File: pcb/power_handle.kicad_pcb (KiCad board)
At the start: 2 copper layers, 115 x 32 mm, 58 parts, among them J1 PJ-202A, J2 USB_C_Receptacle_USB2.0, Q1 PSMN6R0-25YLB, Q2 PSMN6R0-25YLB, Q3 BSS214NW, SW1 SW_SPST, U1 MCP73831T-2ATI/OT, U2 PAM2423, U3 BQ29703DSET

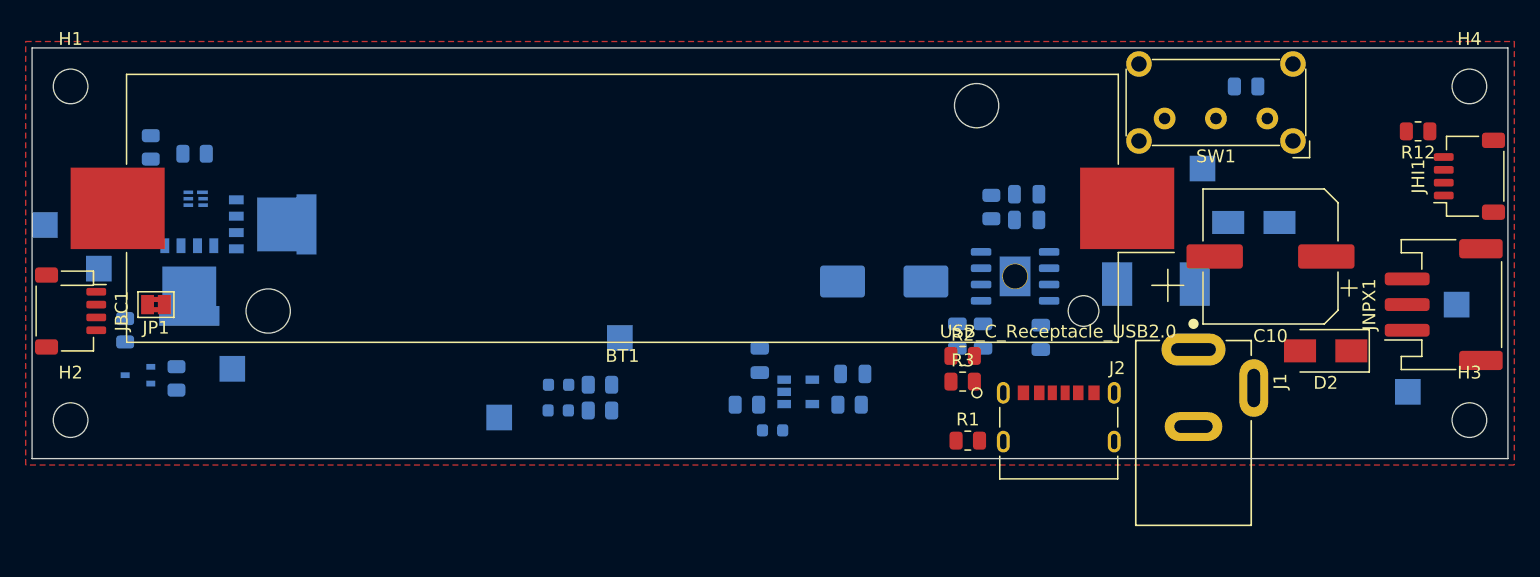
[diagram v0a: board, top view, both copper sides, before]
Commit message: pcb: redo power handle layout
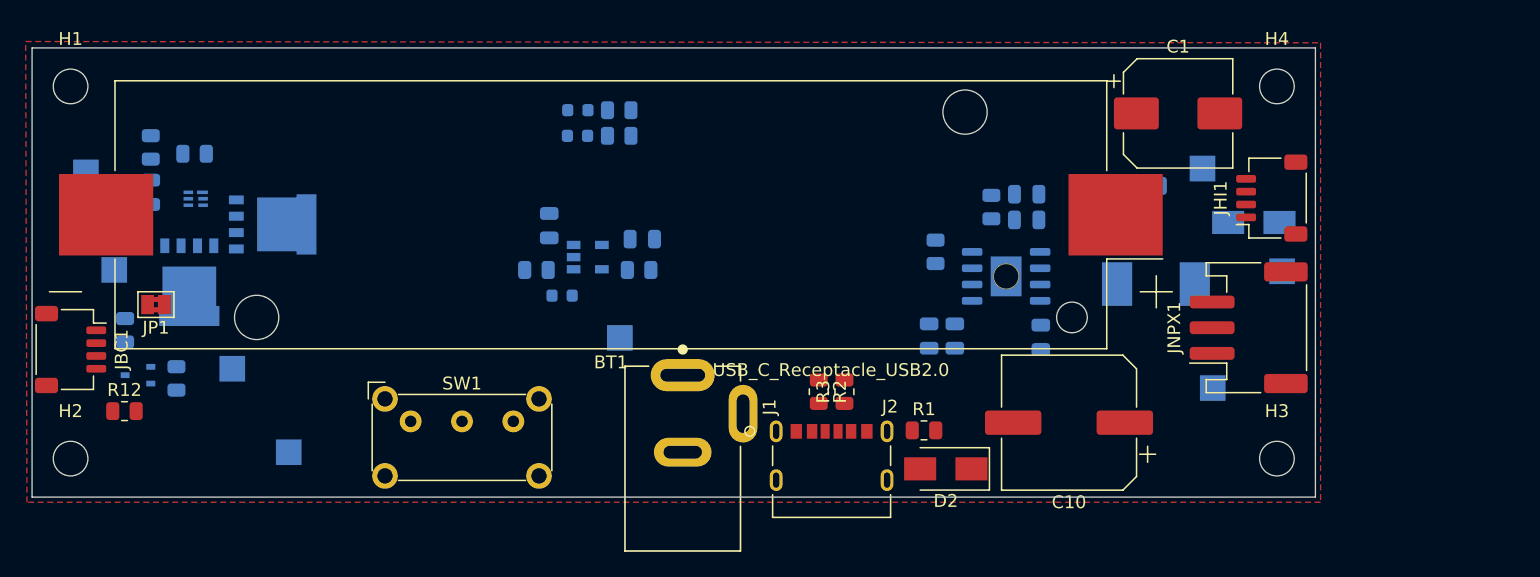
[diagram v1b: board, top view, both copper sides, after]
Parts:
- C1: moved to F.Cu
- moved R12 103.1 mm to (7.20, 28.3), turned to 0 degrees
- moved SW1 70.8 mm to (29.5, 29.1), turned to 0 degrees
- moved J1 39.9 mm to (50.7, 32.0)
- moved D2 31.0 mm to (71.2, 32.8)
- moved R5 27.4 mm to (70.4, 15.9), turned to 270 degrees
- moved C1 26.4 mm to (89.3, 5.10), turned to 0 degrees
- moved D5 21.5 mm to (42.5, 6.85)
- moved D6 21.5 mm to (42.5, 4.85)
- moved R15 21.5 mm to (45.8, 6.85)
- moved R16 21.5 mm to (45.8, 4.85)
- moved C10 20.4 mm to (80.8, 29.2)
- moved C6 19.5 mm to (47.5, 14.9)
- moved C7 19.5 mm to (40.3, 13.8)
- moved D3 19.5 mm to (41.3, 19.3)
- moved R4 19.5 mm to (47.3, 17.3)
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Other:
- board size 115 x 32 mm -> 100 x 35 mm

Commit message: pcb: finish routing of power handle
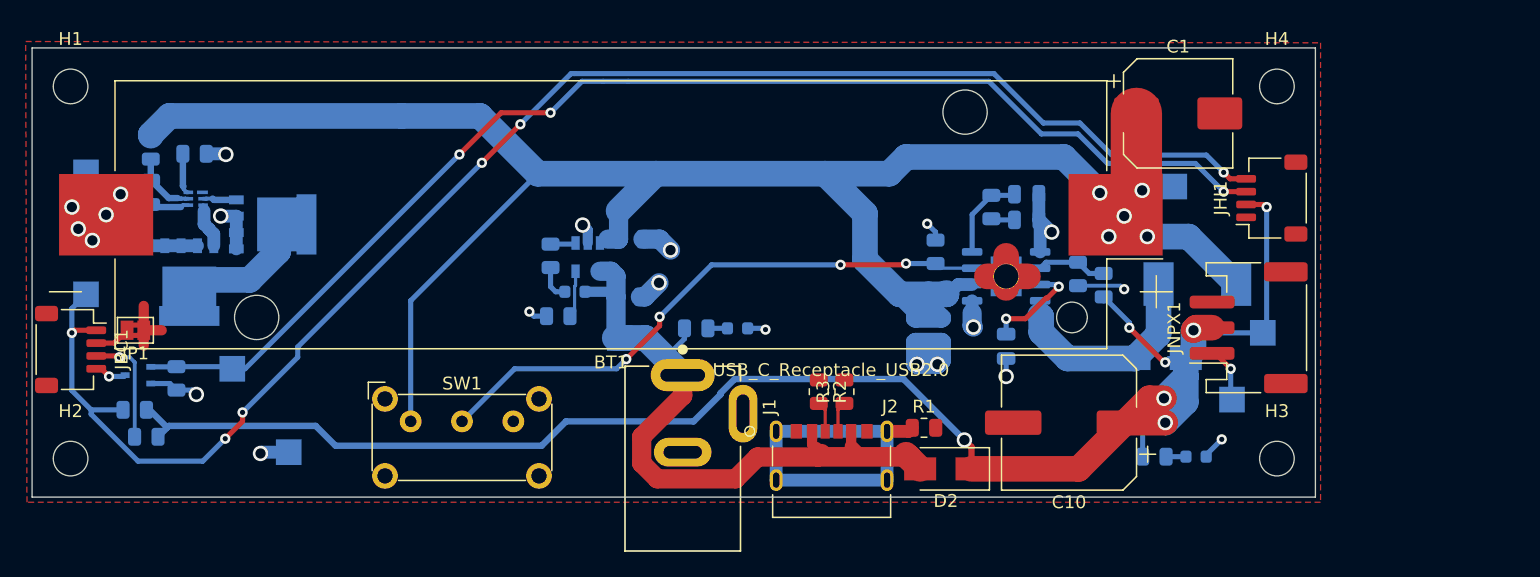
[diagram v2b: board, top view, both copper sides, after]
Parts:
- R12: moved to B.Cu
- moved D5 54.3 mm to (90.7, 31.9), turned to 180 degrees
- moved R15 48.6 mm to (87.5, 31.9), turned to 180 degrees
- moved D6 21.1 mm to (55.0, 21.9), turned to 180 degrees
- moved R16 18.0 mm to (51.8, 21.9), turned to 180 degrees
- moved D4 12.9 mm to (87.9, 24.2)
- moved R9 8.79 mm to (81.5, 17.6), turned to 90 degrees
- moved R13 8.46 mm to (8.90, 30.3), turned to 0 degrees
- moved R8 7.74 mm to (83.5, 18.5), turned to 270 degrees
- moved R4 7.26 mm to (41.0, 20.9), turned to 180 degrees
- moved C7 6.44 mm to (46.6, 14.9), turned to 0 degrees
- moved TP1 5.03 mm to (95.9, 22.2)
- moved C6 4.63 mm to (46.5, 19.4)
- moved L1 3.22 mm to (90.8, 18.4)
- moved TP6 2.91 mm to (4.20, 19.2)
- moved C8 2.79 mm to (75.9, 23.2)
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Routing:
- net +BATT: track 0.00 -> 164.3 mm, vias 0 -> 5
- net VCC: track 0.00 -> 135.5 mm, vias 0 -> 7
- net BTN+: track 0.00 -> 123.2 mm, vias 0 -> 6
- net IC_BTN_LED: track 0.00 -> 98.3 mm, vias 0 -> 3
- net VBUS: track 0.00 -> 62.7 mm
- net GND: track 0.00 -> 56.9 mm, vias 0 -> 17
- net OUTEN: track 0.00 -> 45.5 mm, vias 0 -> 4
- net -BATT: track 0.00 -> 27.9 mm, vias 0 -> 5
- net Net-(J2-PadS1): track 0.00 -> 27.0 mm
- net Net-(D4-Pad2): track 0.00 -> 17.4 mm
- net Net-(Q1-Pad5): track 0.00 -> 10.2 mm
- net LED+: track 0.00 -> 9.01 mm, vias 0 -> 1
- net Net-(C8-Pad2): track 0.00 -> 7.85 mm, vias 0 -> 2
- net Net-(C5-Pad1): track 0.00 -> 6.87 mm
- net Net-(R8-Pad1): track 0.00 -> 5.51 mm
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
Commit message: pcb: cleanup power handle silkscreen, edge cuts
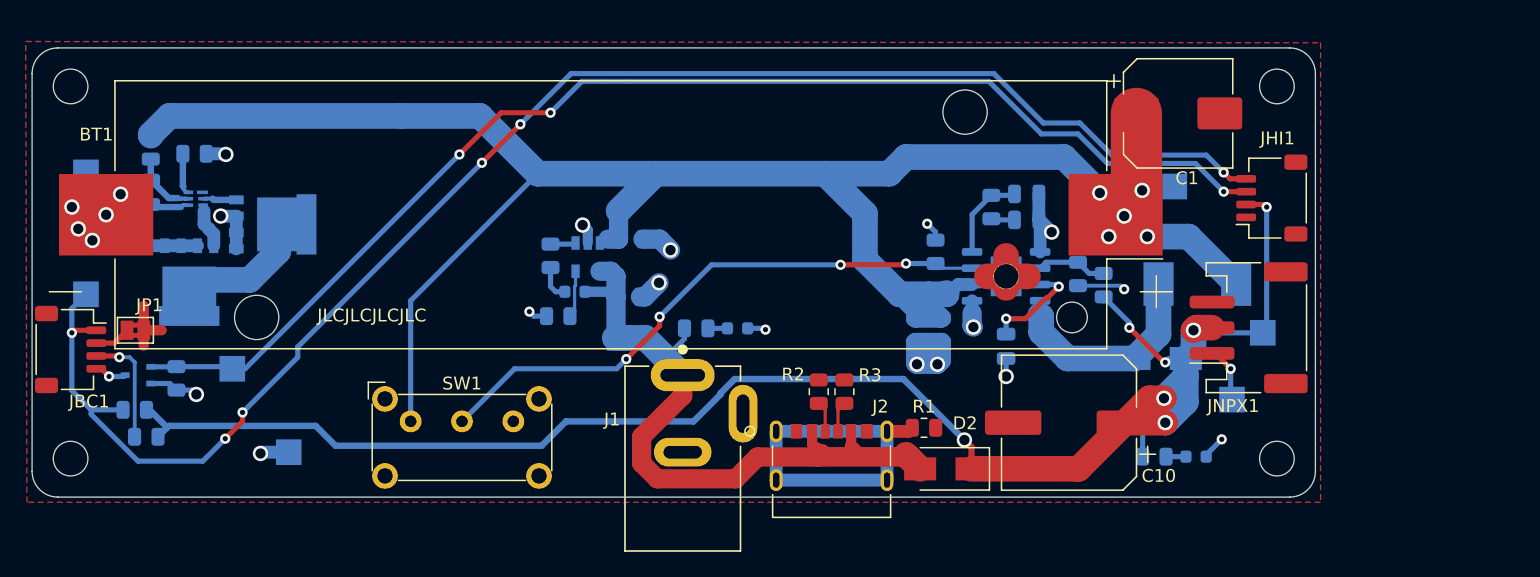
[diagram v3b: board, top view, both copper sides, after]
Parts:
- added LOGO1: Logo_Open_Hardware_Small, Symbol:OSHW-Logo_5.7x6mm_SilkScreen, B.Cu at (27.1, 6.28)
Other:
- outline, holes or cut-outs redrawn
- board text added: "JLCJLCJLCJLC"
- board text added: "LitePog Power Board Rev 1 For use with unprotected cells"

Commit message: pcb: Add testpoint labels to power handle
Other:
- board text added: "+BATT"
- board text added: "-BATT"
- board text added: "BTN+"
- board text added: "GND"
- board text added: "IC_BTN_LED"
- board text added: "NPX_DATA"
- board text added: "VBUS"
- board text added: "VCC 5V"

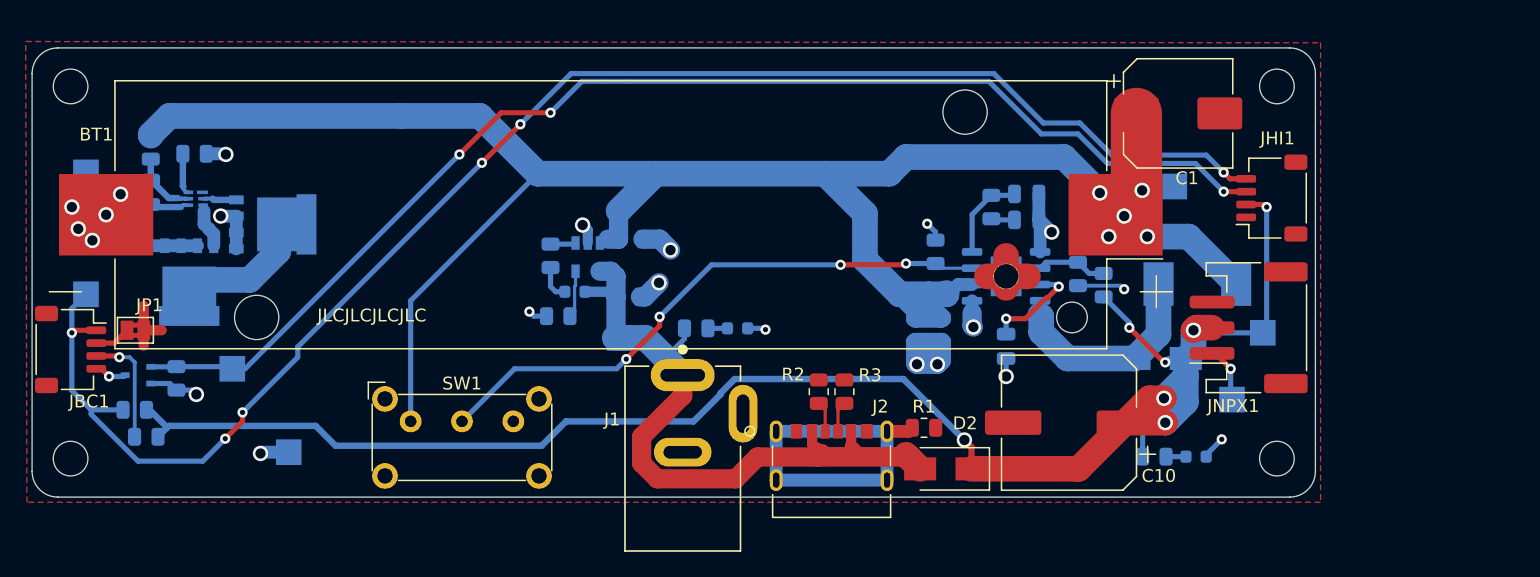
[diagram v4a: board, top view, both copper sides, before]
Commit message: power_handle: Add second ground layer, more info on silkscreen (#3)
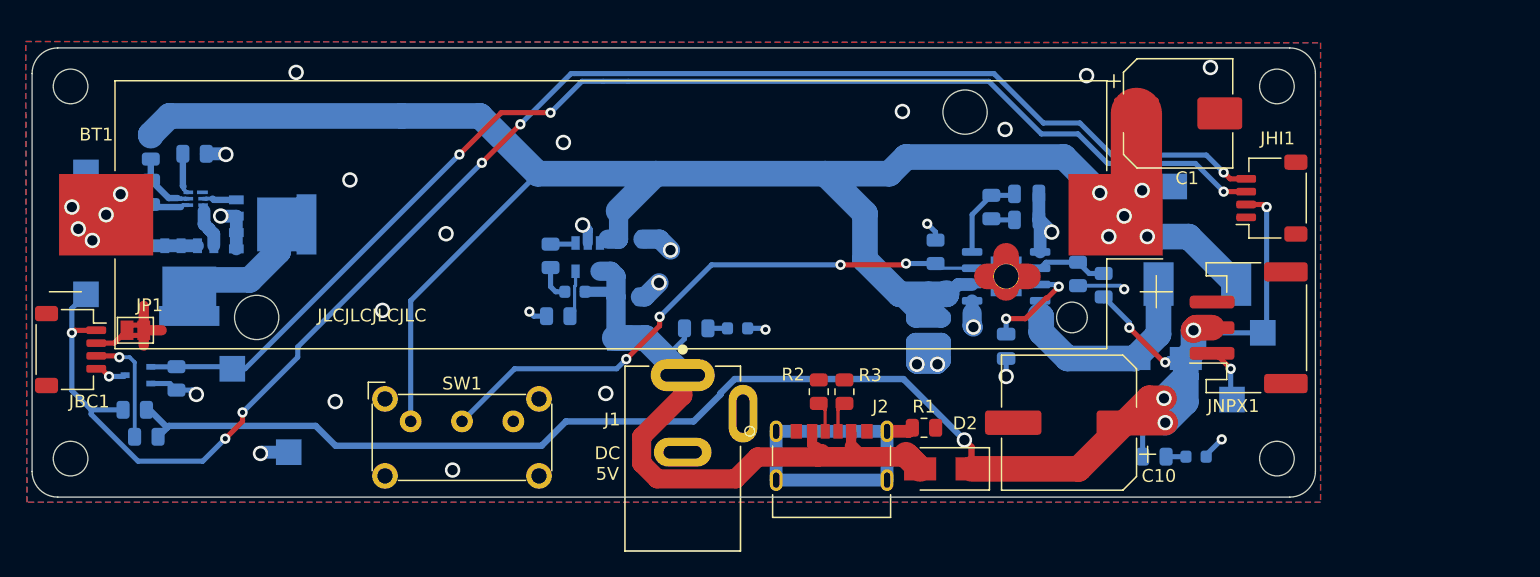
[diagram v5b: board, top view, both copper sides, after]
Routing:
- net GND: vias 17 -> 29
- added copper zone on B.Cu, net GND
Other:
- board text added: "DC 5V"
- board text added: "DO NOT USE USB AND BARREL JACK AT THE SAME TIME"
- board text added: "OFF"
- board text added: "ON"

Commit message: pcb: implement improvements described in rev 1 bringup notes (#23)
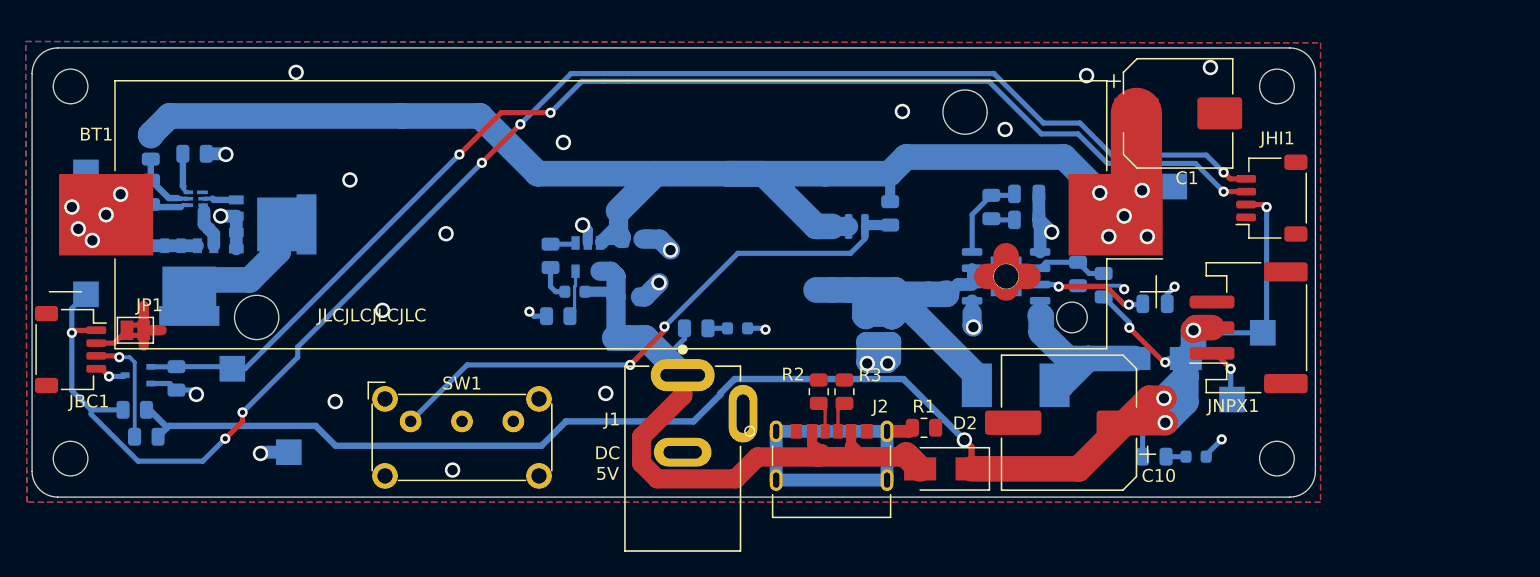
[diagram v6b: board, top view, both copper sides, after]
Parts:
- added Q4: IRF7404, Package_SO:SOIC-8_3.9x4.9mm_P1.27mm, B.Cu at (63.0, 16.4)
- moved L1 16.2 mm to (76.6, 26.3), turned to 0 degrees
- moved C8 12.1 mm to (87.5, 19.9), turned to 180 degrees
- moved R5 4.63 mm to (66.9, 12.9)
- moved C2 3.87 mm to (65.0, 21.9)
- moved C4 3.87 mm to (67.0, 21.9)
- moved C7 0.34 mm to (47.0, 14.9)
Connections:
- C2 pad 2: +BATT -> Net-(C2-Pad2)
- C4 pad 2: +BATT -> Net-(C2-Pad2)
- L1 pad 1: +BATT -> Net-(C2-Pad2)
- R5 pad 1: GND -> +BATT
- R5 pad 2: OUTEN -> Net-(Q4-Pad4)
- SW1 pad 1: +BATT -> Net-(Q4-Pad4)
- SW1 pad 2: OUTEN -> GND
- U2 pad 2: +BATT -> Net-(C2-Pad2)
- U2 pad 3: OUTEN -> Net-(C2-Pad2)
- U3 pad 1: Net-(U3-Pad1) -> (no net)
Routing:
- net OUTEN: track 45.5 -> 0.00 mm, vias 4 -> 0
- net Net-(Q4-Pad4): track 0.00 -> 44.4 mm, vias 0 -> 2
- net +BATT: track 164.3 -> 125.6 mm
- net Net-(C2-Pad2): track 0.00 -> 32.7 mm
- net Net-(D4-Pad2): track 17.4 -> 14.3 mm
- net GND: track 56.9 -> 55.5 mm, vias 29 -> 28
- net Net-(C8-Pad2): track 7.85 -> 8.68 mm
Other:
- board text added: "LitePog Power Board Rev 2 For use with unprotected cells"
- board text removed: "LitePog Power Board Rev 1 For use with unprotected cells"

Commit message: Revert "pcb: implement improvements described in rev 1 bringup notes (#23)"
This reverts commit 01e55846632a9cef383a24172751afed95ee1909.
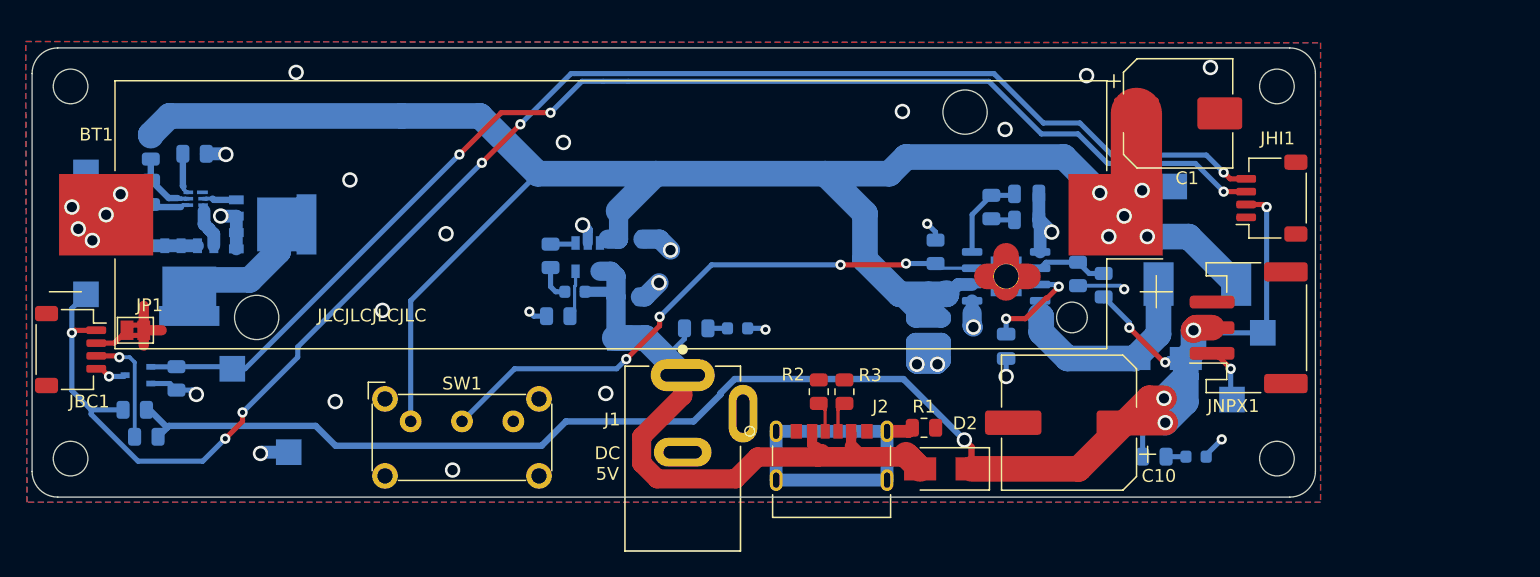
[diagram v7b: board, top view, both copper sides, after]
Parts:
- removed Q4: IRF7404, Package_SO:SOIC-8_3.9x4.9mm_P1.27mm
- moved L1 16.2 mm to (90.8, 18.4), turned to 180 degrees
- moved C8 12.1 mm to (75.9, 23.2), turned to 90 degrees
- moved R5 4.63 mm to (70.4, 15.9)
- moved C2 3.87 mm to (68.8, 22.0)
- moved C4 3.87 mm to (70.8, 22.0)
- moved C7 0.34 mm to (46.6, 14.9)
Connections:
- C2 pad 2: Net-(C2-Pad2) -> +BATT
- C4 pad 2: Net-(C2-Pad2) -> +BATT
- L1 pad 1: Net-(C2-Pad2) -> +BATT
- R5 pad 1: +BATT -> GND
- R5 pad 2: Net-(Q4-Pad4) -> OUTEN
- SW1 pad 1: Net-(Q4-Pad4) -> +BATT
- SW1 pad 2: GND -> OUTEN
- U2 pad 2: Net-(C2-Pad2) -> +BATT
- U2 pad 3: Net-(C2-Pad2) -> OUTEN
- U3 pad 1: (no net) -> Net-(U3-Pad1)
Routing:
- net OUTEN: track 0.00 -> 45.5 mm, vias 0 -> 4
- net Net-(Q4-Pad4): track 44.4 -> 0.00 mm, vias 2 -> 0
- net +BATT: track 125.6 -> 164.3 mm
- net Net-(C2-Pad2): track 32.7 -> 0.00 mm
- net Net-(D4-Pad2): track 14.3 -> 17.4 mm
- net GND: track 55.5 -> 56.9 mm, vias 28 -> 29
- net Net-(C8-Pad2): track 8.68 -> 7.85 mm
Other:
- board text added: "LitePog Power Board Rev 1 For use with unprotected cells"
- board text removed: "LitePog Power Board Rev 2 For use with unprotected cells"
